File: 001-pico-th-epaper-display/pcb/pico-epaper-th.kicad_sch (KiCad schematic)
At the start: 10 parts, among them Q1 AO3407, U1 GY-SHT31-D, U2 TPL5110, U3 WS_1_54_epaper_module

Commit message: name change
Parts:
- added C4: 100n, Capacitor_SMD:C_0603_1608Metric_Pad1.08x0.95mm_HandSolder, symbol Device:C
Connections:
- net GND: now also C4.2
- net VCC: now also R1.1, U2.3 (DELAY/M_DRV)
- net at A1.39 (VSYS), C1.1, Q1.3 (D): now also C4.1
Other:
- moved on the sheet: C1, C2, R1, U2

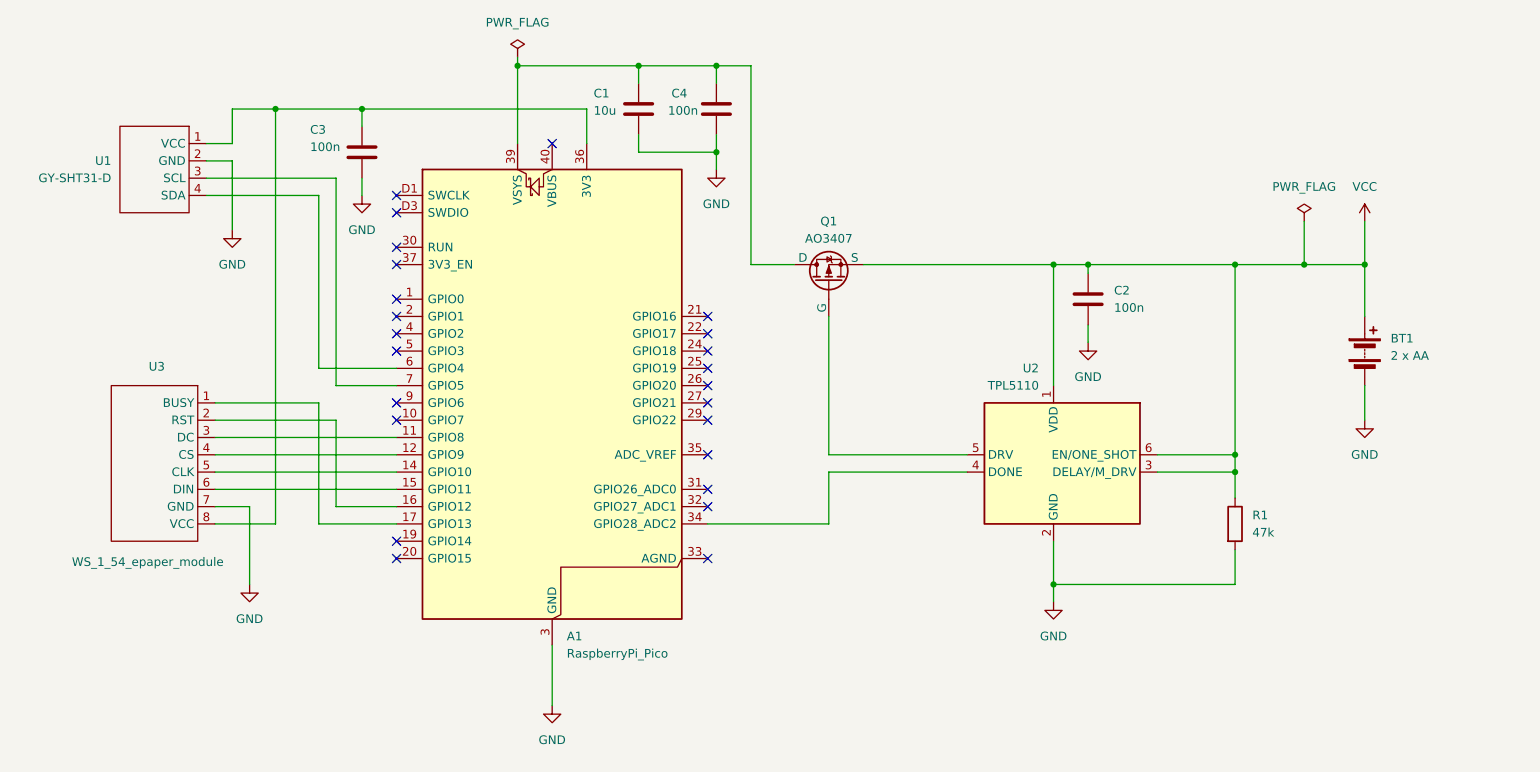
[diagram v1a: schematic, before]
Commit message: pin changed for sht31
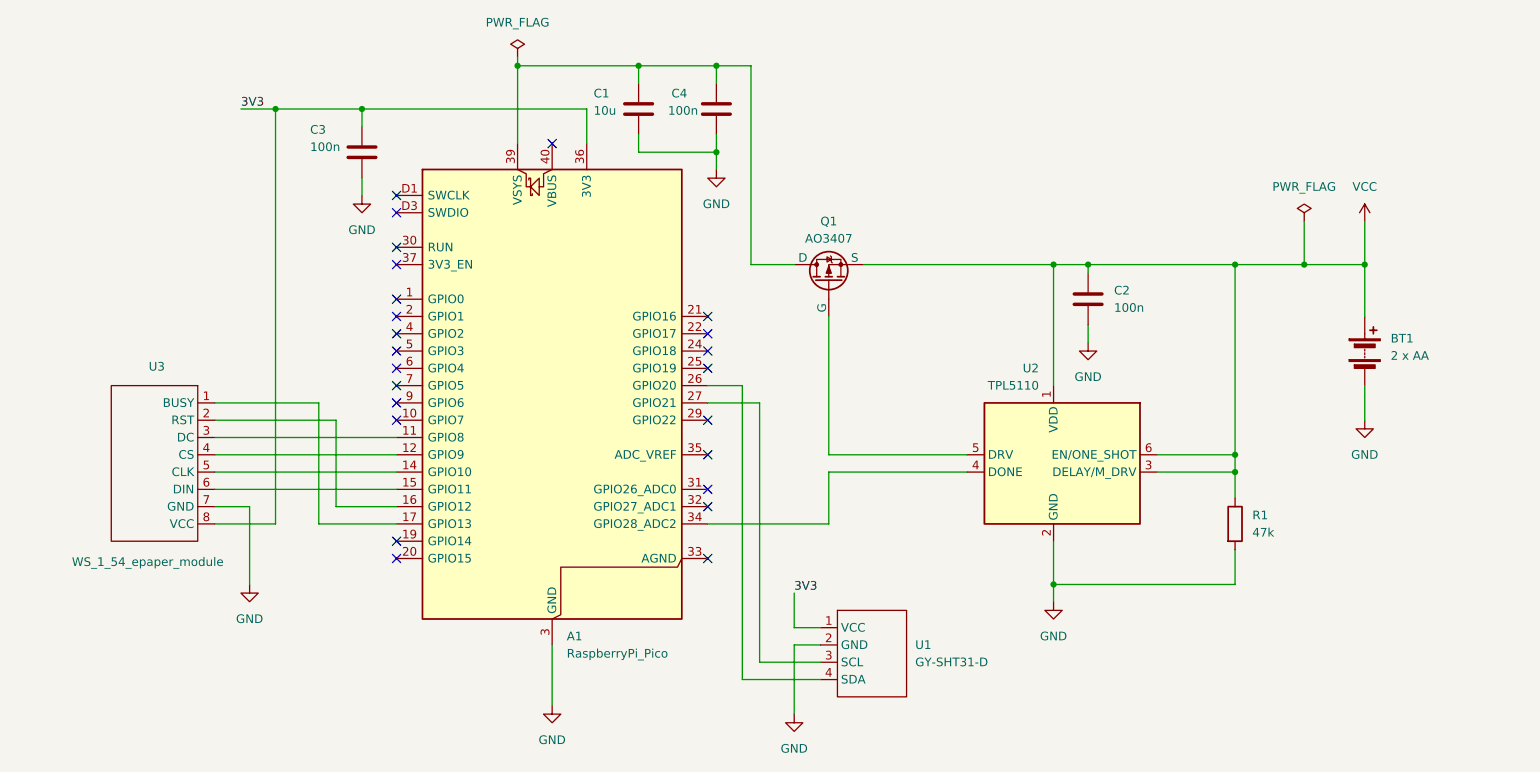
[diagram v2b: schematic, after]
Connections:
- net 3V3: now reaches A1.36 (3V3), C3.1, U1.1 (VCC), U3.8 (VCC)
- net at U1.3 (SCL): now also A1.27 (GPIO21); no longer A1.7 (GPIO5)
- net at U1.4 (SDA): now also A1.26 (GPIO20); no longer A1.6 (GPIO4)
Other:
- moved on the sheet: U1
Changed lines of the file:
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@@
+	)
+	(junction
+		(at 62.23 53.34)
+		(diameter 0)
+		(color 0 0 0 0)
 	)
 	(junction
@@
 		(color 0 0 0 0)
 	)
-	(junction
-		(at 62.23 53.34)
-		(diameter 0)
-		(color 0 0 0 0)
-	)
 	(no_connect
 		(at 80.01 116.84)
@@
 	)
 	(no_connect
+		(at 80.01 93.98)
+	)
+	(no_connect
 		(at 125.73 88.9)
+	)
+	(no_connect
+		(at 80.01 91.44)
 	)
 	(no_connect
@@
 	)
 	(no_connect
-		(at 125.73 93.98)
-	)
-	(no_connect
 		(at 125.73 111.76)
 	)
@@
 	)
 	(no_connect
-		(at 125.73 96.52)
-	)
-	(no_connect
 		(at 125.73 86.36)
 	)
@@
 	(wire
 		(pts
-			(xy 52.07 60.96) (xy 55.88 60.96)
+			(xy 142.24 132.08) (xy 138.43 132.08)
+		)
+		(stroke
+			(width 0)
+			(type default)
+		)
+	)
+	(wire
+		(pts
+			(xy 57.15 53.34) (xy 62.23 53.34)
 		)
 		(stroke
@@
 	(wire
 		(pts
-			(xy 71.12 93.98) (xy 80.01 93.98)
-		)
-		(stroke
-			(width 0)
-			(type default)
-		)
-	)
-	(wire
-		(pts
-			(xy 55.88 53.34) (xy 62.23 53.34)
-		)
-		(stroke
-			(width 0)
-			(type default)
-		)
-	)
-	(wire
-		(pts
 			(xy 97.79 45.72) (xy 97.79 46.99)
 		)
@@
 	(wire
 		(pts
+			(xy 125.73 96.52) (xy 133.35 96.52)
+		)
+		(stroke
+			(width 0)
+			(type default)
+		)
+	)
+	(wire
+		(pts
 			(xy 53.34 99.06) (xy 71.12 99.06)
 		)
@@
 	(wire
 		(pts
+			(xy 130.81 137.16) (xy 130.81 93.98)
+		)
+		(stroke
+			(width 0)
+			(type default)
+		)
+	)
+	(wire
+		(pts
 			(xy 132.08 76.2) (xy 138.43 76.2)
 		)
@@
 	(wire
 		(pts
-			(xy 68.58 91.44) (xy 80.01 91.44)
-		)
-		(stroke
-			(width 0)
-			(type default)
-		)
-	)
-	(wire
-		(pts
 			(xy 102.87 132.08) (xy 102.87 140.97)
 		)
@@
 	(wire
 		(pts
-			(xy 68.58 66.04) (xy 68.58 91.44)
-		)
-		(stroke
-			(width 0)
-			(type default)
-		)
-	)
-	(wire
-		(pts
-			(xy 52.07 63.5) (xy 71.12 63.5)
-		)
-		(stroke
-			(width 0)
-			(type default)
-		)
-	)
-	(wire
-		(pts
 			(xy 203.2 76.2) (xy 203.2 104.14)
 		)
@@
 	(wire
 		(pts
+			(xy 133.35 134.62) (xy 142.24 134.62)
+		)
+		(stroke
+			(width 0)
+			(type default)
+		)
+	)
+	(wire
+		(pts
 			(xy 143.51 114.3) (xy 125.73 114.3)
 		)
@@
 	(wire
 		(pts
-			(xy 52.07 58.42) (xy 55.88 58.42)
+			(xy 142.24 129.54) (xy 138.43 129.54)
 		)
 		(stroke
@@
 	(wire
 		(pts
-			(xy 52.07 66.04) (xy 68.58 66.04)
-		)
-		(stroke
-			(width 0)
-			(type default)
-		)
-	)
-	(wire
-		(pts
 			(xy 213.36 69.85) (xy 213.36 76.2)
 		)
@@
 	(wire
 		(pts
+			(xy 130.81 93.98) (xy 125.73 93.98)
+		)
+		(stroke
+			(width 0)
+			(type default)
+		)
+	)
+	(wire
+		(pts
 			(xy 97.79 46.99) (xy 97.79 58.42)
 		)
@@
 	(wire
 		(pts
+			(xy 130.81 137.16) (xy 142.24 137.16)
+		)
+		(stroke
+			(width 0)
+			(type default)
+		)
+	)
+	(wire
+		(pts
 			(xy 115.57 57.15) (xy 115.57 59.69)
 		)
@@
 	(wire
 		(pts
-			(xy 55.88 60.96) (xy 55.88 71.12)
+			(xy 138.43 132.08) (xy 138.43 142.24)
 		)
 		(stroke
@@
 	(wire
 		(pts
-			(xy 55.88 58.42) (xy 55.88 53.34)
+			(xy 138.43 129.54) (xy 138.43 124.46)
 		)
 		(stroke
@@
 	(wire
 		(pts
-			(xy 71.12 63.5) (xy 71.12 93.98)
-		)
-		(stroke
-			(width 0)
-			(type default)
-		)
-	)
-	(wire
-		(pts
 			(xy 222.25 69.85) (xy 222.25 76.2)
 		)
@@
 	(wire
 		(pts
+			(xy 133.35 96.52) (xy 133.35 134.62)
+		)
+		(stroke
+			(width 0)
+			(type default)
+		)
+	)
+	(wire
+		(pts
 			(xy 74.93 63.5) (xy 74.93 66.04)
 		)
@@
 			(width 0)
 			(type default)
+		)
+	)
+	(label "3V3"
+		(at 138.43 124.46 0)
+		(effects
+			(font
+				(size 1.27 1.27)
+			)
+			(justify left bottom)
+		)
+	)
+	(label "3V3"
+		(at 57.15 53.34 0)
+		(effects
+			(font
+				(size 1.27 1.27)
+			)
+			(justify left bottom)
 		)
 	)
 	(symbol
 		(lib_id "electronut:GY-SHT31-D")
-		(at 44.45 60.96 0)
-		(mirror y)
+		(at 149.86 132.08 0)
 		(unit 1)
 		(body_style 1)
@@
 		(dnp no)
 		(property "Reference" "U1"
-			(at 38.1 60.9599 0)
+			(at 156.21 132.0799 0)
 			(show_name no)
 			(do_not_autoplace no)
@@
 		)
 		(property "Value" "GY-SHT31-D"
-			(at 38.1 63.4999 0)
+			(at 156.21 134.6199 0)
 			(show_name no)
 			(do_not_autoplace no)
@@
 		)
 		(property "Footprint" "Connector_PinHeader_2.54mm:PinHeader_1x04_P2.54mm_Vertical"
-			(at 44.45 60.96 0)
+			(at 149.86 132.08 0)
 			(hide yes)
 			(show_name no)
@@
 		)
 		(property "Datasheet" ""
-			(at 44.45 60.96 0)
+			(at 149.86 132.08 0)
 			(hide yes)
 			(show_name no)
@@
 		)
 		(property "Description" "Temp/Humidity I2C Module"
-			(at 43.942 73.152 0)
+			(at 150.368 144.272 0)
 			(hide yes)
 			(show_name no)
@@
 		)
 		(property "Notes" "Pull-ups onboard"
-			(at 44.704 75.438 0)
+			(at 149.606 146.558 0)
 			(hide yes)
 			(show_name no)
@@
 	(symbol
 		(lib_id "power:GND")
-		(at 55.88 71.12 0)
+		(at 138.43 142.24 0)
+		(mirror y)
 		(unit 1)
 		(body_style 1)
@@
 		(fields_autoplaced yes)
 		(property "Reference" "#PWR06"
-			(at 55.88 77.47 0)
+			(at 138.43 148.59 0)
 			(hide yes)
 			(show_name no)
@@
 		)
 		(property "Value" "GND"
-			(at 55.88 76.2 0)
+			(at 138.43 147.32 0)
 			(show_name no)
 			(do_not_autoplace no)
@@
 		)
 		(property "Footprint" ""
-			(at 55.88 71.12 0)
+			(at 138.43 142.24 0)
 			(hide yes)
 			(show_name no)
@@
 		)
 		(property "Datasheet" ""
-			(at 55.88 71.12 0)
+			(at 138.43 142.24 0)
 			(hide yes)
 			(show_name no)
@@
 		)
 		(property "Description" "Power symbol creates a global label with name \"GND\" , ground"
-			(at 55.88 71.12 0)
-			(hide yes)
-			(show_name no)
+			(at 138.43 142.24 0)
+			(hide yes)
+			(show_name no)

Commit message: schematic updated
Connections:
- net VCC: no longer R1.1, U2.3 (DELAY/M_DRV)
- new net: R1.1, U2.3 (DELAY/M_DRV)
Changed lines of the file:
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@@
-	)
-	(junction
-		(at 203.2 104.14)
-		(diameter 0)
-		(color 0 0 0 0)
 	)
 	(junction
@@
 	(junction
 		(at 181.61 76.2)
-		(diameter 0)
-		(color 0 0 0 0)
-	)
-	(junction
-		(at 203.2 106.68)
 		(diameter 0)
 		(color 0 0 0 0)
@@
 		)
 		(stroke
-			(width 0)
-			(type default)
-		)
-	)
-	(wire
-		(pts
-			(xy 203.2 104.14) (xy 203.2 106.68)
-		)
-		(stroke

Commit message: updated pcb
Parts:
- C1: value 10u -> 0.1u
- C2, C3: value 100n -> 0.1u
- C4: value 100n -> 10u
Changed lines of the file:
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@@
 			)
 		)
-		(property "Value" "100n"
+		(property "Value" "10u"
 			(at 119.888 53.594 0)
 			(show_name no)
@@
 			)
 		)
-		(property "Value" "10u"
+		(property "Value" "0.1u"
 			(at 108.966 53.594 0)
 			(show_name no)
@@
 			)
 		)
-		(property "Value" "100n"
+		(property "Value" "0.1u"
 			(at 67.31 58.928 0)
 			(show_name no)
@@
 			)
 		)
-		(property "Value" "100n"
+		(property "Value" "0.1u"
 			(at 185.42 82.5499 0)
 			(show_name no)

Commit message: removed locked silk
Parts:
- BT1: value 2 x AA -> 3 x AA (4.5 V)
- Q1: value AO3407 -> DMG3415U
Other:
- note added: "R1 sets the timer delay. 47k is about 6 mins. Set as per TPL5110 datasheet."
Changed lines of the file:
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@@
 		(comment 1 "Mahesh Venkitachalam")
+	)
+	(text "R1 sets the timer delay. \n47k is about 6 mins. \nSet as per TPL5110 datasheet."
+		(exclude_from_sim no)
+		(at 210.82 114.046 0)
+		(effects
+			(font
+				(size 1.27 1.27)
+			)
+			(justify left)
+		)
 	)
 	(junction
@@
 			)
 		)
-		(property "Value" "AO3407"
+		(property "Value" "DMG3415U"
 			(at 143.51 72.39 90)
 			(show_name no)
@@
 			)
 		)
-		(property "Value" "2 x AA"
+		(property "Value" "3 x AA (4.5 V)"
 			(at 226.06 89.5984 0)
 			(show_name no)

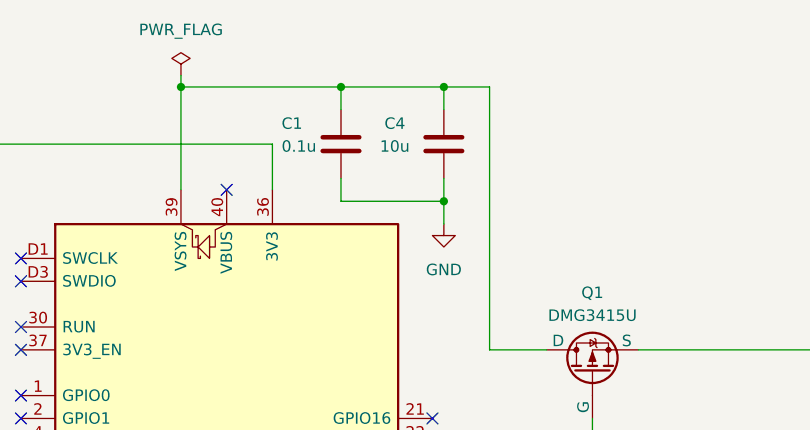
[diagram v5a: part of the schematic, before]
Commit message: turn leds off
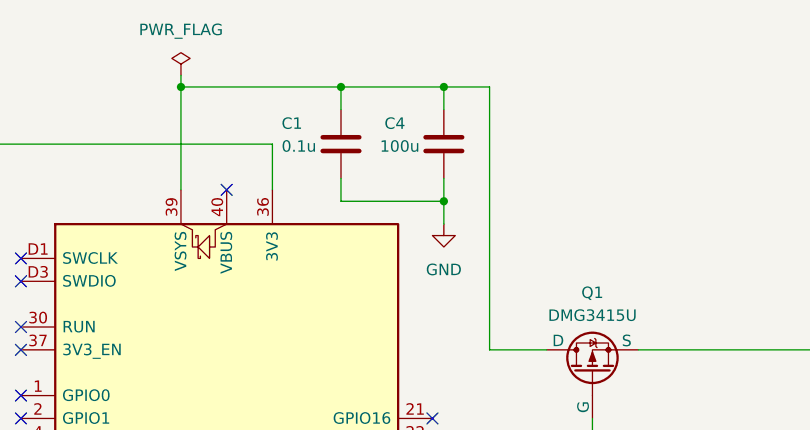
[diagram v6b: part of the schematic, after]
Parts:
- C4: value 10u -> 100u
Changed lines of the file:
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@@
 			)
 		)
-		(property "Value" "10u"
+		(property "Value" "100u"
 			(at 119.888 53.594 0)
 			(show_name no)
